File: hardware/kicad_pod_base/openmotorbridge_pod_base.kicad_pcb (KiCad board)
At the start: 2 copper layers, 36 x 20 mm, 6 parts

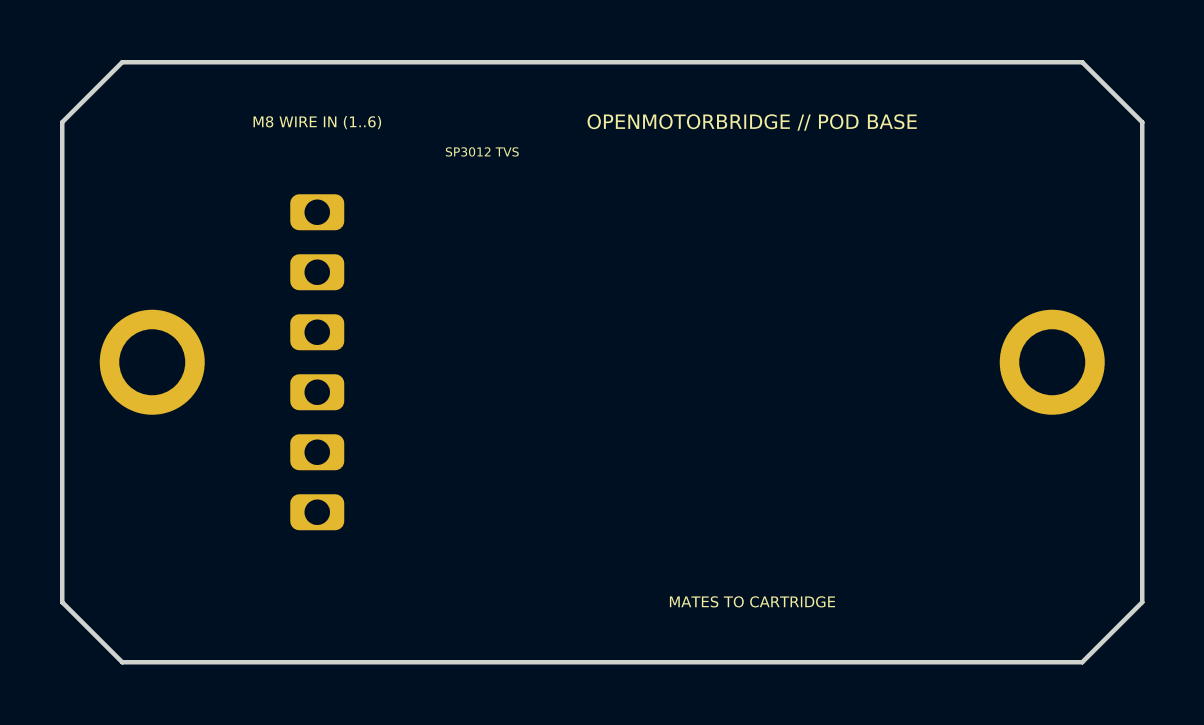
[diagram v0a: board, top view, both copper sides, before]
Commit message: hardware(pod_base): revert to integrated M8 direct PCB mount design
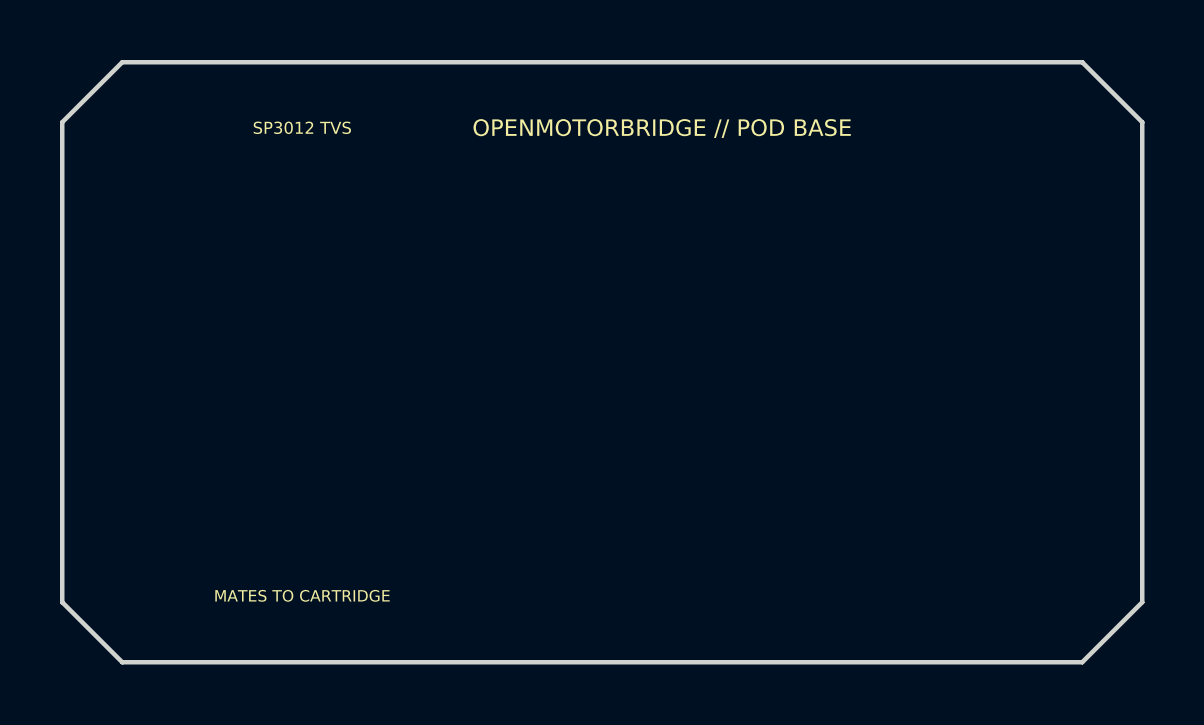
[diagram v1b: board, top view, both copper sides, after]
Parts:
- J2: moved to B.Cu
- moved J2 10.7 mm to (118.0, 80.0)
- moved C1 5.52 mm to (108.0, 84.0)
- moved U1 5.52 mm to (108.0, 76.0)
- moved J1 2.00 mm to (118.0, 73.7)
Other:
- board text added: "GND SHIELD PLANE"
- board text added: "M8 6-PIN IP67 (OUTSIDE)"
- board text removed: "GND SHIELD PLANE // 0 HOLES IN MATING ZONE"
- board text removed: "M8 WIRE IN (1..6)"
- board text removed: "OPENMOTORBRIDGE POD BASE (B.Cu)"

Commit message: hardware(pod_base/cad): implement Variante A (panel-mount M8 with O-ring, locknut and wire leads, eliminating THT pin collisions)
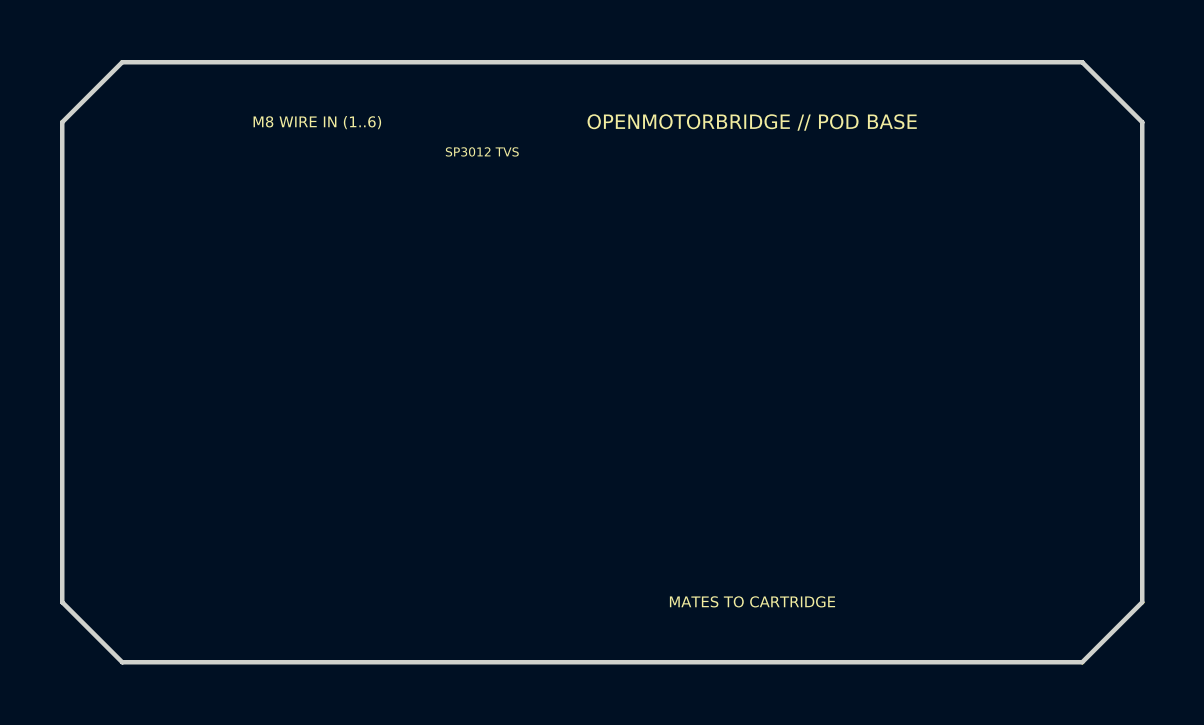
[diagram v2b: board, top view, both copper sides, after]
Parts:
- J2: moved to F.Cu
- moved J2 10.7 mm to (108.5, 75.0)
- moved C1 5.52 mm to (113.5, 83.5)
- moved U1 5.52 mm to (113.5, 76.5)
- moved J1 2.00 mm to (120.0, 73.7)
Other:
- board text added: "GND SHIELD PLANE // 0 HOLES IN MATING ZONE"
- board text added: "M8 WIRE IN (1..6)"
- board text added: "OPENMOTORBRIDGE POD BASE (B.Cu)"
- board text removed: "GND SHIELD PLANE"
- board text removed: "M8 6-PIN IP67 (OUTSIDE)"
